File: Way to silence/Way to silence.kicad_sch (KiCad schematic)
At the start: 17 parts, among them J3 5V_Terminal, J4 Battery_Terminal, J5 LEDS Port, SW1 SW_SPDT, SW3 SW_SPST, U1 ESP32-WROOM-32-N16, U6 AMS1117CD-3.3

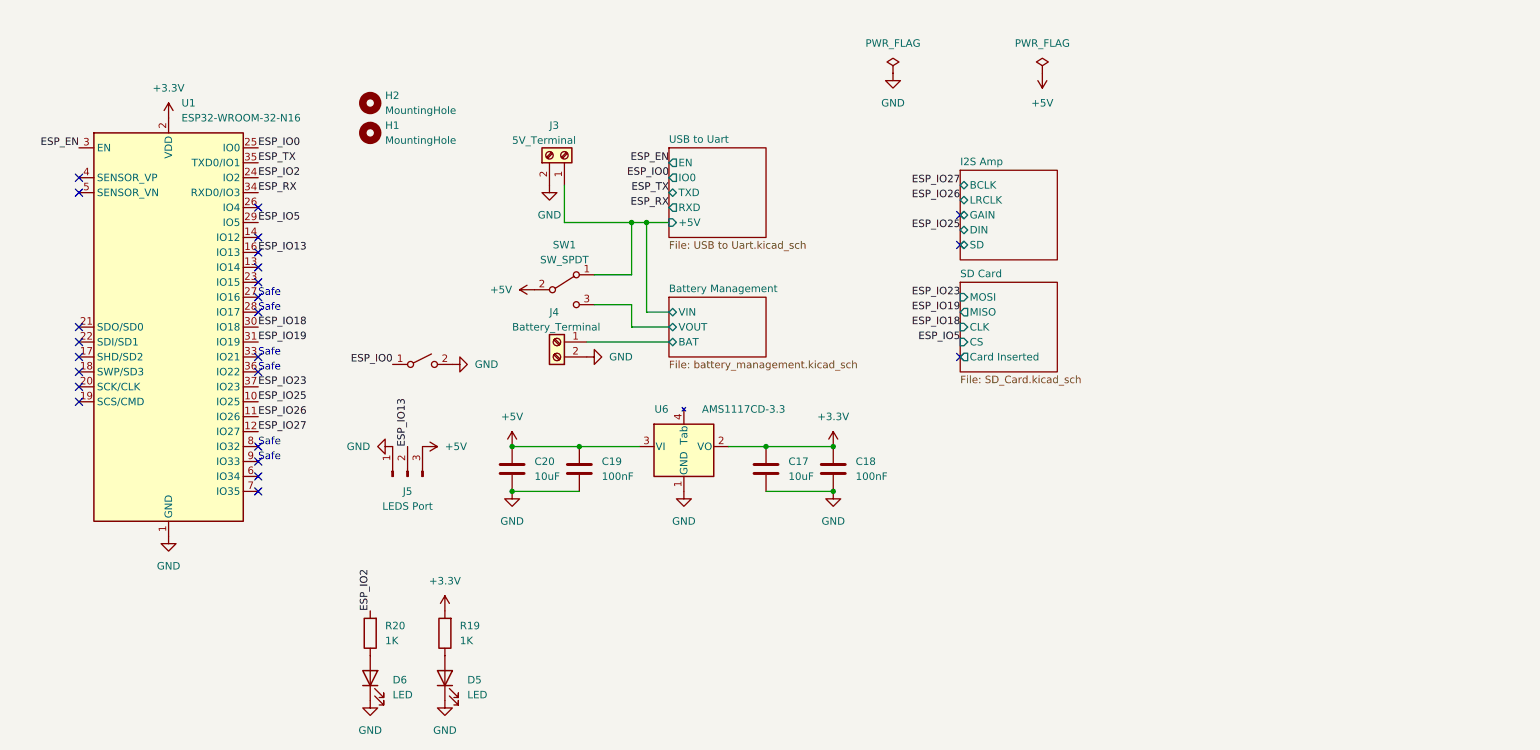
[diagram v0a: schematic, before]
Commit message: [ADD] Styles to shematics
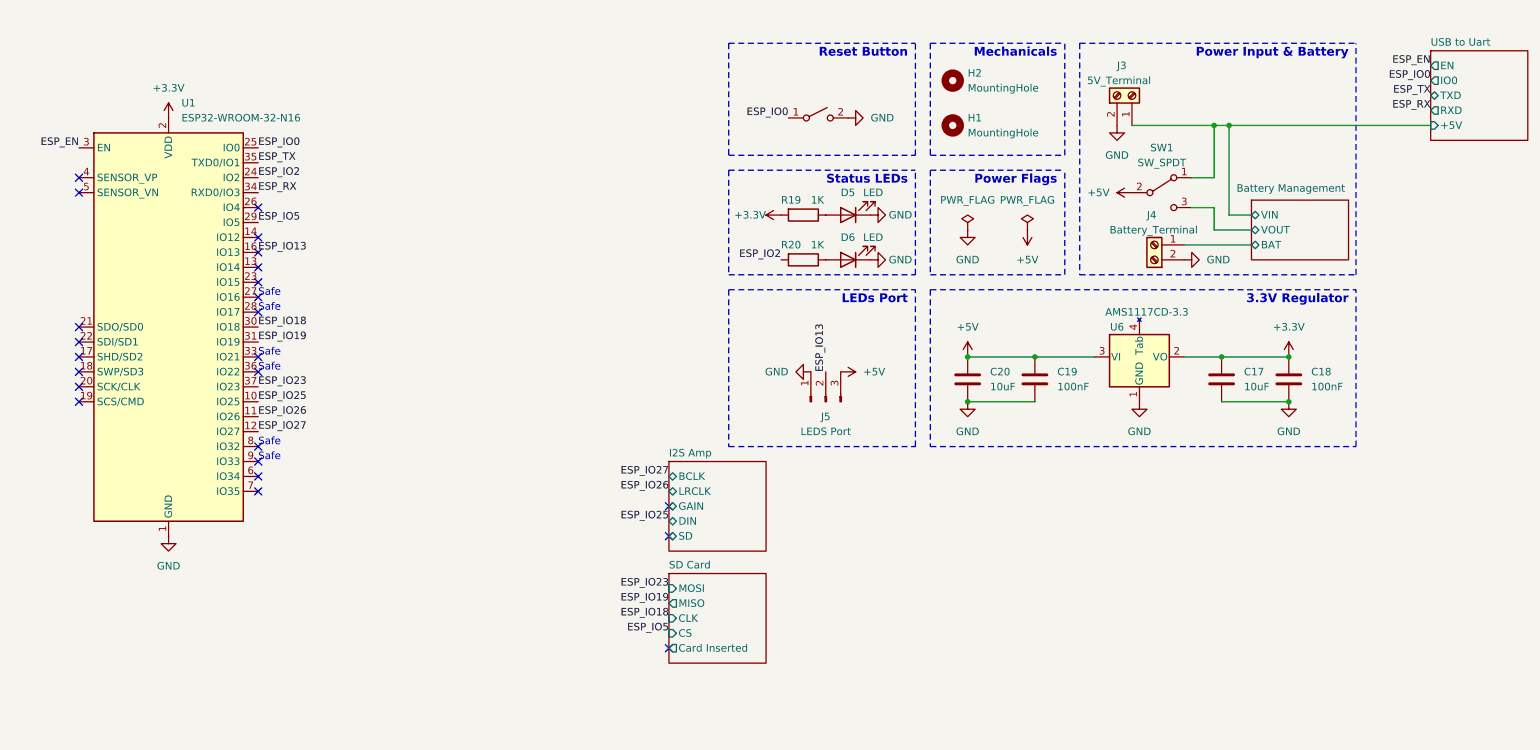
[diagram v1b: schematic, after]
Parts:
- J5: footprint (none) -> Way to silence:PinHeader_1x03_P2.54mm_Vertical
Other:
- note added: "3.3V Regulator"
- note added: "LEDs Port"
- note added: "Mechanicals"
- note added: "Power Flags"
- note added: "Power Input & Battery"
- note added: "Reset Button"
- note added: "Status LEDs"
- moved on the sheet: C17, C18, C19, C20, D5, D6, H1, H2, J3, J4, J5, R19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

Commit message: [ADD] Root page style
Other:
- note added: "Microcontroller"
- moved on the sheet: C17, C18, C19, C20, D5, D6, H1, H2, J3, J4, J5, R19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

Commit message: [ADD] Shematics files settings
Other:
- title: (none) -> Way To Silence
- moved on the sheet: C17, C18, C19, C20, D5, D6, H1, H2, J3, J4, J5, R19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

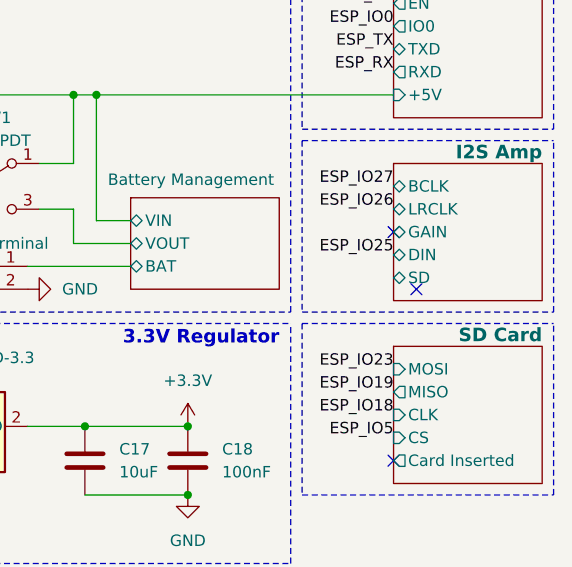
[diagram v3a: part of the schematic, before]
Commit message: [ERC] 1 Warning cleaned
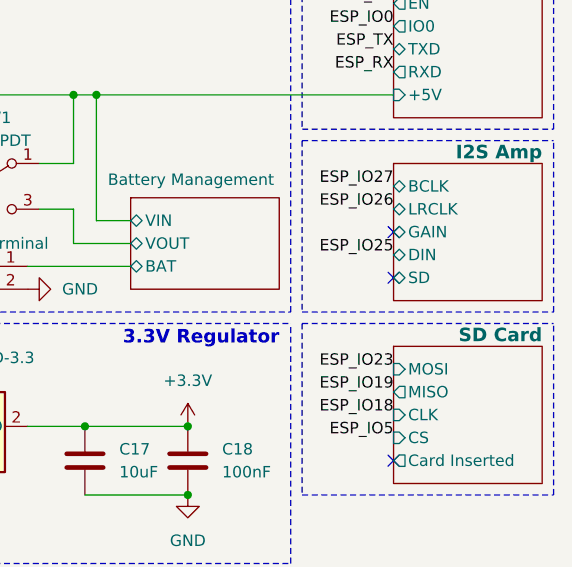
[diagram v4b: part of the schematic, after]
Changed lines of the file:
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@@
   (no_connect (at 19.05 58.42))
   (no_connect (at 49.53 63.5))
-  (no_connect (at 180.34 52.07))
+  (no_connect (at 177.8 50.8))
   (no_connect (at 49.53 81.28))
   (no_connect (at 177.8 71.12))

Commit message: [UDPT] Leds colors
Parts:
- D5, D6: LCSC C84263 -> C84268
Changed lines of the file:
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@@
       (effects (font (size 1.27 1.27)) hide)
     )
-    (property "LCSC" "C84263" (at 81.28 57.15 0)
+    (property "LCSC" "C84268" (at 81.28 57.15 0)
       (effects (font (size 1.27 1.27)) hide)
     )
@@
       (effects (font (size 1.27 1.27)) hide)
     )
-    (property "LCSC" "C84263" (at 81.28 49.53 0)
+    (property "LCSC" "C84268" (at 81.28 49.53 0)
       (effects (font (size 1.27 1.27)) hide)
     )

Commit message: [UDPT] Sheet name
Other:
- sheet Battery Management renamed BMS
- moved on the sheet: J4, SW1
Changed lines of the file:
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@@
     (rev "1.0")
   )
-  (junction (at 144.78 30.48) (diameter 0) (color 0 0 0 0)
-  )
-  (junction (at 142.24 30.48) (diameter 0) (color 0 0 0 0)
-  )
   (junction (at 143.51 67.31) (diameter 0) (color 0 0 0 0)
   )
   (junction (at 100.33 67.31) (diameter 0) (color 0 0 0 0)
   )
+  (junction (at 143.51 30.48) (diameter 0) (color 0 0 0 0)
+  )
   (junction (at 111.76 67.31) (diameter 0) (color 0 0 0 0)
   )
   (junction (at 154.94 67.31) (diameter 0) (color 0 0 0 0)
+  )
+  (junction (at 140.97 30.48) (diameter 0) (color 0 0 0 0)
   )
   (junction (at 154.94 74.93) (diameter 0) (color 0 0 0 0)
@@
     (stroke (width 0) (type dash))
   )
-  (wire (pts (xy 148.59 46.99) (xy 142.24 46.99))
+  (wire (pts (xy 143.51 30.48) (xy 177.8 30.48))
+    (stroke (width 0) (type default))
+  )
+  (wire (pts (xy 148.59 46.99) (xy 140.97 46.99))
     (stroke (width 0) (type default))
   )
@@
     (stroke (width 0) (type dash))
   )
-  (wire (pts (xy 138.43 38.1) (xy 142.24 38.1))
+  (wire (pts (xy 137.16 38.1) (xy 140.97 38.1))
     (stroke (width 0) (type default))
   )
@@
     (stroke (width 0) (type dash))
   )
-  (wire (pts (xy 142.24 30.48) (xy 128.27 30.48))
+  (wire (pts (xy 140.97 30.48) (xy 143.51 30.48))
     (stroke (width 0) (type default))
   )
@@
     (stroke (width 0) (type dash))
   )
-  (wire (pts (xy 144.78 44.45) (xy 148.59 44.45))
+  (wire (pts (xy 143.51 44.45) (xy 148.59 44.45))
     (stroke (width 0) (type default))
   )
@@
     (stroke (width 0) (type dash))
   )
-  (wire (pts (xy 142.24 46.99) (xy 142.24 43.18))
+  (wire (pts (xy 140.97 46.99) (xy 140.97 43.18))
     (stroke (width 0) (type default))
   )
@@
     (stroke (width 0) (type dash))
   )
-  (wire (pts (xy 142.24 38.1) (xy 142.24 30.48))
+  (wire (pts (xy 140.97 38.1) (xy 140.97 30.48))
     (stroke (width 0) (type default))
   )
@@
     (stroke (width 0) (type dash))
   )
+  (polyline (pts (xy 166.37 35.56) (xy 146.05 35.56))
+    (stroke (width 0) (type dash))
+  )
   (wire (pts (xy 100.33 74.93) (xy 111.76 74.93))
     (stroke (width 0) (type default))
@@
     (stroke (width 0) (type dash))
   )
-  (wire (pts (xy 142.24 30.48) (xy 144.78 30.48))
-    (stroke (width 0) (type default))
-  )
   (polyline (pts (xy 60.96 15.24) (xy 60.96 34.29))
     (stroke (width 0) (type dash))
@@
     (stroke (width 0) (type dash))
   )
+  (wire (pts (xy 134.62 52.07) (xy 137.16 52.07))
+    (stroke (width 0) (type default))
+  )
   (polyline (pts (xy 167.64 74.93) (xy 195.58 74.93))
     (stroke (width 0) (type dash))
@@
     (stroke (width 0) (type dash))
   )
-  (wire (pts (xy 144.78 30.48) (xy 144.78 44.45))
+  (wire (pts (xy 143.51 30.48) (xy 143.51 44.45))
     (stroke (width 0) (type default))
   )
@@
     (stroke (width 0) (type dash))
   )
+  (polyline (pts (xy 146.05 35.56) (xy 146.05 54.61))
+    (stroke (width 0) (type dash))
+  )
   (polyline (pts (xy 195.58 74.93) (xy 195.58 55.88))
     (stroke (width 0) (type dash))
@@
     (stroke (width 0) (type dash))
   )
-  (wire (pts (xy 137.16 49.53) (xy 148.59 49.53))
+  (wire (pts (xy 134.62 49.53) (xy 148.59 49.53))
     (stroke (width 0) (type default))
   )
@@
     (stroke (width 0) (type default))
   )
+  (wire (pts (xy 140.97 30.48) (xy 128.27 30.48))
+    (stroke (width 0) (type default))
+  )
   (polyline (pts (xy 92.71 34.29) (xy 92.71 15.24))
     (stroke (width 0) (type dash))
@@
     (stroke (width 0) (type dash))
   )
-  (wire (pts (xy 144.78 30.48) (xy 177.8 30.48))
-    (stroke (width 0) (type default))
-  )
   (polyline (pts (xy 93.98 82.55) (xy 166.37 82.55))
     (stroke (width 0) (type dash))
@@
     (stroke (width 0) (type dash))
   )
-  (wire (pts (xy 142.24 43.18) (xy 138.43 43.18))
+  (wire (pts (xy 140.97 43.18) (xy 137.16 43.18))
     (stroke (width 0) (type default))
   )
@@
     )
   )
-  (symbol (lib_id "power:+5V") (at 128.27 40.64 90) (unit 1)
-    (in_bom yes) (on_board yes) (dnp no) (fields_autoplaced)
-    (property "Reference" "#PWR06" (at 132.08 40.64 0)
-      (effects (font (size 1.27 1.27)) hide)
-    )
-    (property "Value" "+5V" (at 124.46 40.64 90)
-      (effects (font (size 1.27 1.27)) (justify left))
-    )
-    (property "Footprint" "" (at 128.27 40.64 0)
-      (effects (font (size 1.27 1.27)) hide)
-    )
-    (property "Datasheet" "" (at 128.27 40.64 0)
+  (symbol (lib_id "power:+5V") (at 127 40.64 90) (unit 1)
+    (in_bom yes) (on_board yes) (dnp no) (fields_autoplaced)
+    (property "Reference" "#PWR06" (at 130.81 40.64 0)
+      (effects (font (size 1.27 1.27)) hide)
+    )
+    (property "Value" "+5V" (at 123.19 40.64 90)
+      (effects (font (size 1.27 1.27)) (justify left))
+    )
+    (property "Footprint" "" (at 127 40.64 0)
+      (effects (font (size 1.27 1.27)) hide)
+    )
+    (property "Datasheet" "" (at 127 40.64 0)
       (effects (font (size 1.27 1.27)) hide)
     )
@@
     )
   )
-  (symbol (lib_id "Way to silence:SW_SPDT") (at 133.35 40.64 0) (unit 1)
-    (in_bom yes) (on_board yes) (dnp no) (fields_autoplaced)
-    (property "Reference" "SW1" (at 133.35 33.02 0)
-      (effects (font (size 1.27 1.27)))
-    )
-    (property "Value" "SW_SPDT" (at 133.35 35.56 0)
-      (effects (font (size 1.27 1.27)))
-    )
-    (property "Footprint" "Way to silence:SW_SPDT" (at 132.08 26.67 0)
-      (effects (font (size 1.27 1.27)) hide)
-    )
-    (property "Datasheet" "~" (at 133.35 29.21 0)
-      (effects (font (size 1.27 1.27)) hide)
-    )
-    (property "LCSC" "C319013" (at 132.08 24.13 0)
+  (symbol (lib_id "Way to silence:SW_SPDT") (at 132.08 40.64 0) (unit 1)
+    (in_bom yes) (on_board yes) (dnp no) (fields_autoplaced)
+    (property "Reference" "SW1" (at 132.08 33.02 0)
+      (effects (font (size 1.27 1.27)))
+    )
+    (property "Value" "SW_SPDT" (at 132.08 35.56 0)
+      (effects (font (size 1.27 1.27)))
+    )
+    (property "Footprint" "Way to silence:SW_SPDT" (at 130.81 26.67 0)
+      (effects (font (size 1.27 1.27)) hide)
+    )
+    (property "Datasheet" "~" (at 132.08 29.21 0)
+      (effects (font (size 1.27 1.27)) hide)
+    )
+    (property "LCSC" "C319013" (at 130.81 24.13 0)
       (effects (font (size 1.27 1.27)) hide)
     )
@@
     )
   )
-  (symbol (lib_id "Way to silence:Screw_Terminal_01x02") (at 132.08 52.07 180) (unit 1)
+  (symbol (lib_id "Way to silence:Screw_Terminal_01x02") (at 129.54 52.07 180) (unit 1)
     (in_bom yes) (on_board yes) (dnp no)
-    (property "Reference" "J4" (at 130.81 44.45 0)
-      (effects (font (size 1.27 1.27)) (justify right))
-    )
-    (property "Value" "Battery_Terminal" (at 124.46 46.99 0)
-      (effects (font (size 1.27 1.27)) (justify right))
-    )
-    (property "Footprint" "Way to silence:Screw_Terminal_3.5" (at 132.08 52.07 0)
-      (effects (font (size 1.27 1.27)) hide)
-    )
-    (property "Datasheet" "~" (at 132.08 52.07 0)
-      (effects (font (size 1.27 1.27)) hide)
-    )
-    (property "LCSC" "C784942" (at 132.08 58.42 0)
+    (property "Reference" "J4" (at 128.27 44.45 0)
+      (effects (font (size 1.27 1.27)) (justify right))
+    )
+    (property "Value" "Battery_Terminal" (at 121.92 46.99 0)
+      (effects (font (size 1.27 1.27)) (justify right))
+    )
+    (property "Footprint" "Way to silence:Screw_Terminal_3.5" (at 129.54 52.07 0)
+      (effects (font (size 1.27 1.27)) hide)
+    )
+    (property "Datasheet" "~" (at 129.54 52.07 0)
+      (effects (font (size 1.27 1.27)) hide)
+    )
+    (property "LCSC" "C784942" (at 129.54 58.42 0)
       (effects (font (size 1.27 1.27)) hide)
     )
@@
     )
   )
-  (sheet (at 148.59 41.91) (size 16.51 10.16)
+  (sheet (at 148.59 38.1) (size 16.51 15.24)
     (stroke (width 0.1524) (type solid))
     (fill (color 0 0 0 0.0000))
-    (property "Sheetname" "Battery Management" (at 146.05 40.64 0)
-      (effects (font (size 1.27 1.27)) (justify left bottom))
-    )
-    (property "Sheetfile" "battery_management.kicad_sch" (at 148.59 52.6546 0)
+    (property "Sheetname" "BMS" (at 165.1 36.83 0)
+      (effects (font (size 1.5 1.5) bold) (justify right))
+    )
+    (property "Sheetfile" "battery_management.kicad_sch" (at 148.59 48.8446 0)
       (effects (font (size 1.27 1.27)) (justify left top) hide)
     )

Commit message: [ADD] Terminals Rotations
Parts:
- H1, H2: now left out of the parts list
- J3, J4: JLCPCB Rotation Offset (none) -> 180
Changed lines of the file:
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@@
     )
   )
-  (symbol (lib_id "Way to silence:MountingHole") (at 97.79 21.59 0) (unit 1)
-    (in_bom yes) (on_board yes) (dnp no) (fields_autoplaced)
+  (symbol (lib_name "MountingHole_1") (lib_id "Way to silence:MountingHole") (at 97.79 21.59 0) (unit 1)
+    (in_bom no) (on_board yes) (dnp no) (fields_autoplaced)
     (property "Reference" "H2" (at 100.33 20.32 0)
       (effects (font (size 1.27 1.27)) (justify left))
@@
   )
   (symbol (lib_id "Way to silence:MountingHole") (at 97.79 29.21 0) (unit 1)
-    (in_bom yes) (on_board yes) (dnp no) (fields_autoplaced)
+    (in_bom no) (on_board yes) (dnp no) (fields_autoplaced)
     (property "Reference" "H1" (at 100.33 27.94 0)
       (effects (font (size 1.27 1.27)) (justify left))
@@
       (effects (font (size 1.27 1.27)) hide)
     )
+    (property "JLCPCB Rotation Offset" "180" (at 129.54 57.15 0)
+      (effects (font (size 1.27 1.27)) hide)
+    )
     (pin "1")
     (pin "2")
@@
       (effects (font (size 1.27 1.27)) hide)
     )
+    (property "JLCPCB Rotation Offset" "180" (at 120.65 24.13 0)
+      (effects (font (size 1.27 1.27)) hide)
+    )

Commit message: [ADD] U6 Q1 Q2 Rotations
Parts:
- U6: JLCPCB Rotation Offset (none) -> 270
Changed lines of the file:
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@@
+      (effects (font (size 1.27 1.27)) hide)
+    )
+    (property "JLCPCB Rotation Offset" "270" (at 133.35 58.42 0)
       (effects (font (size 1.27 1.27)) hide)
     )
